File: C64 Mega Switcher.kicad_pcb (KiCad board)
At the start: 2 copper layers, 44.2 x 79.5 mm, 20 parts, among them J1 Port 1, J2 Port 2, J3 Mega Drive, J4 C_SEL, J5 B_SEL, SW1 P1_SEL, SW2 P2_SEL, U1 74HCT4053, U2 74HCT4053, U3 NE555

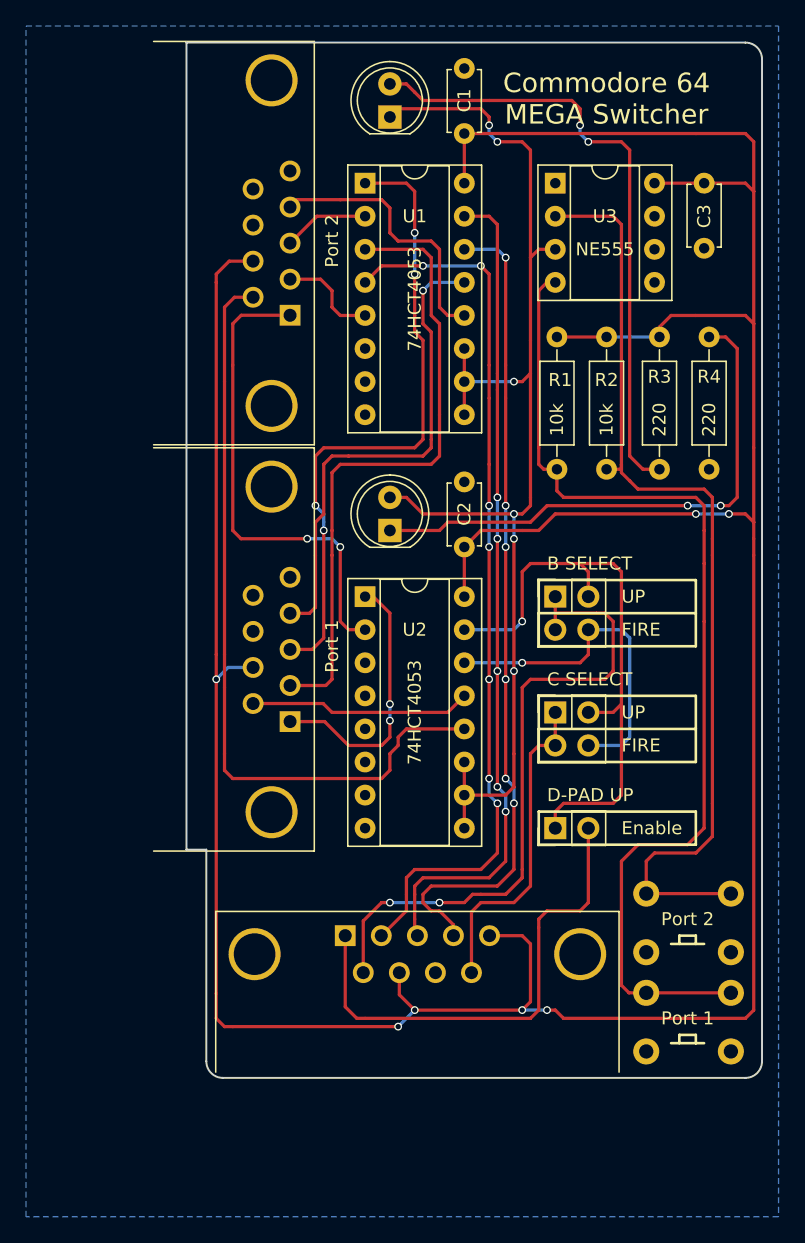
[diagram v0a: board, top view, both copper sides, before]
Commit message: Added protection diodes
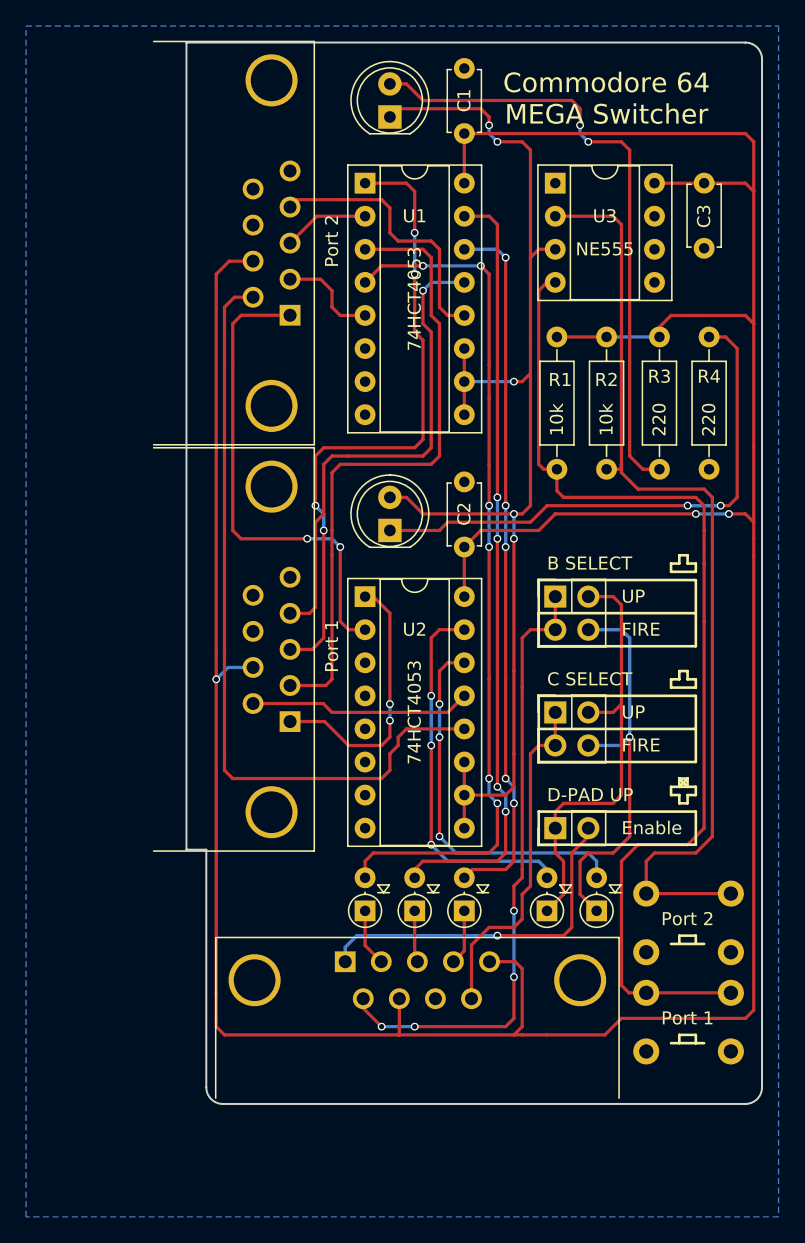
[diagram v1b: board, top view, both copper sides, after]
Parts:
- added D3: 1N4148, Diodes_THT:D_DO-35_SOD27_P2.54mm_Vertical_AnodeUp, F.Cu at (119.4, 102.2)
- added D4: 1N4148, Diodes_THT:D_DO-35_SOD27_P2.54mm_Vertical_AnodeUp, F.Cu at (115.6, 102.2)
- added D5: 1N4148, Diodes_THT:D_DO-35_SOD27_P2.54mm_Vertical_AnodeUp, F.Cu at (111.8, 102.2)
- added D6: 1N4148, Diodes_THT:D_DO-35_SOD27_P2.54mm_Vertical_AnodeUp, F.Cu at (129.5, 102.2)
- added D7: 1N4148, Diodes_THT:D_DO-35_SOD27_P2.54mm_Vertical_AnodeUp, F.Cu at (125.7, 102.2)
- moved J3 2.00 mm to (110.2, 106.1)
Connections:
- J3 pad 2: DOWN -> /MD_D
- J3 pad 3: LEFT -> /MD_L
- J3 pad 4: RIGHT -> /MD_R
- J4 pad 2: UP -> Net-(D7-Pad1)
- J4 pad 4: FIRE -> Net-(D6-Pad1)
- J5 pad 2: UP -> Net-(D7-Pad1)
- J5 pad 4: FIRE -> Net-(D6-Pad1)
- JP1 pad 1: UP -> Net-(D7-Pad1)
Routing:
- net Net-(D7-Pad1): track 0.00 -> 34.2 mm
- net Net-(D6-Pad1): track 0.00 -> 31.1 mm, vias 0 -> 1
- net UP: track 46.3 -> 29.0 mm, vias 1 -> 3
- net /MD_U: track 38.4 -> 27.3 mm, vias 0 -> 1
- net RIGHT: track 63.0 -> 54.4 mm, vias 6 -> 5
- net /MD_D: track 0.00 -> 4.42 mm
- net /MD_R: track 0.00 -> 4.25 mm
- net LEFT: track 63.6 -> 59.5 mm, vias 5 -> 4
- net /MD_L: track 0.00 -> 3.99 mm
- net FIRE: track 26.2 -> 29.0 mm, vias 1 -> 3
- net Net-(J3-Pad6): track 50.7 -> 48.0 mm, vias 2 -> 4
- net DOWN: track 68.1 -> 66.3 mm, vias 7 -> 6
- net Net-(J3-Pad9): track 24.9 -> 26.5 mm
- net VCC: track 263.0 -> 262.2 mm, vias 7 -> 3
- net PORT: vias 6 -> 5
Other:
- board size 44.2 x 79.5 mm -> 44.2 x 81.5 mm

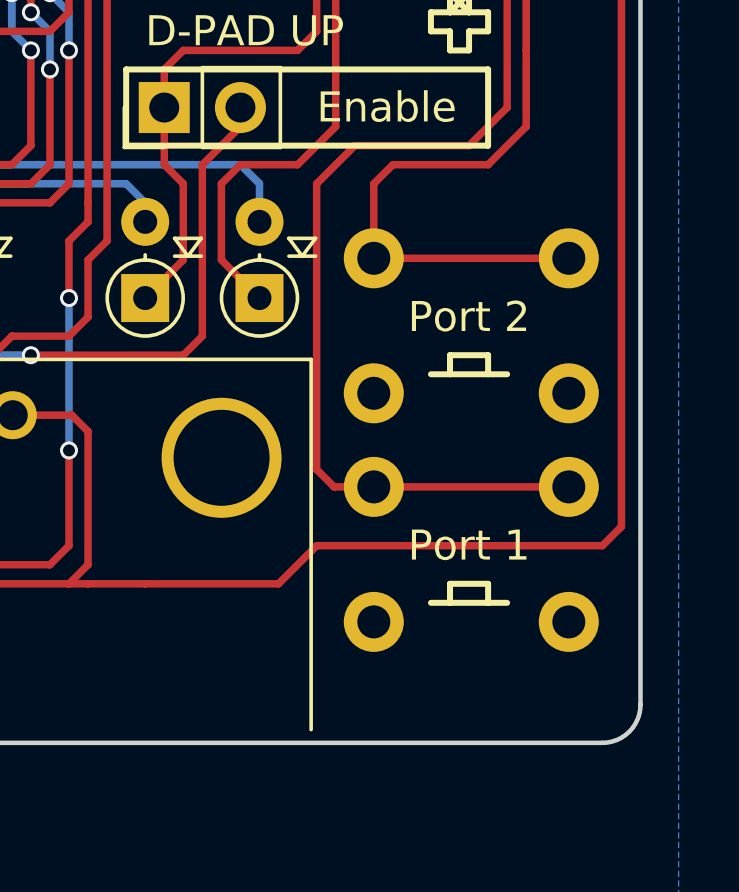
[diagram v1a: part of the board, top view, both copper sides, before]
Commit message: Swapped buttons the right way
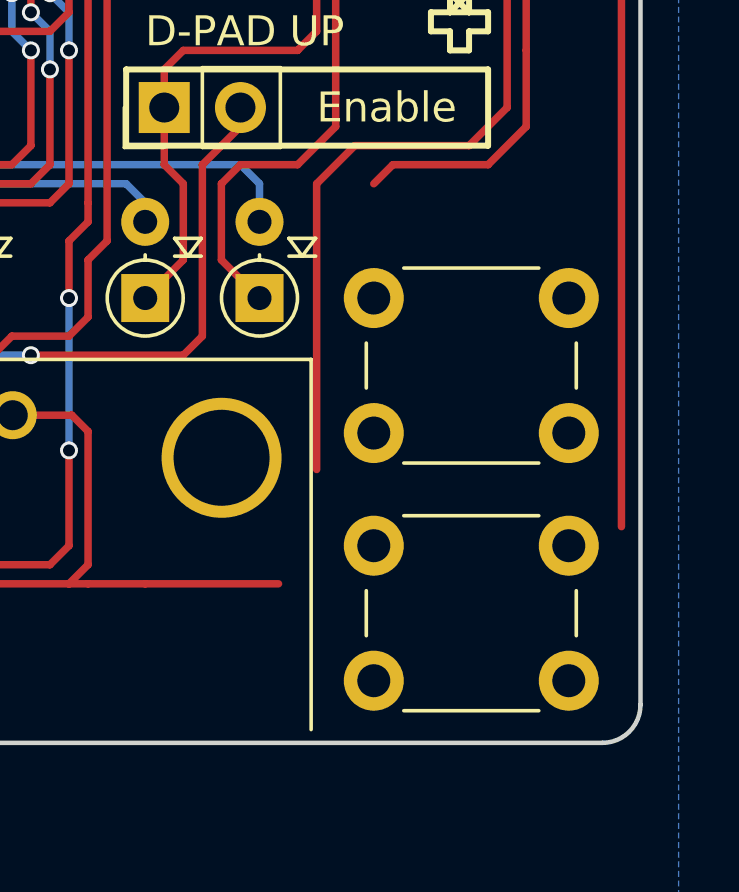
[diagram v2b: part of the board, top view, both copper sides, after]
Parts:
- SW1, SW2: moved to F.Cu
- moved SW2 3.17 mm to (133.3, 102.2)
- moved SW1 2.54 mm to (133.3, 110.5)
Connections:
- SW1 pad 2: Net-(R1-Pad2) -> Net-(R2-Pad2)
- SW2 pad 2: Net-(R2-Pad2) -> Net-(R1-Pad2)
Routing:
- net VCC: track 262.2 -> 250.0 mm
- net Net-(R2-Pad2): track 74.6 -> 65.6 mm
- net Net-(R1-Pad2): track 80.2 -> 71.5 mm
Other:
- board text added: "Licensed under CERN OHL v.1.2 github.com/tebl"
- board text removed: "Licensed under CERN OHL v.1.2"

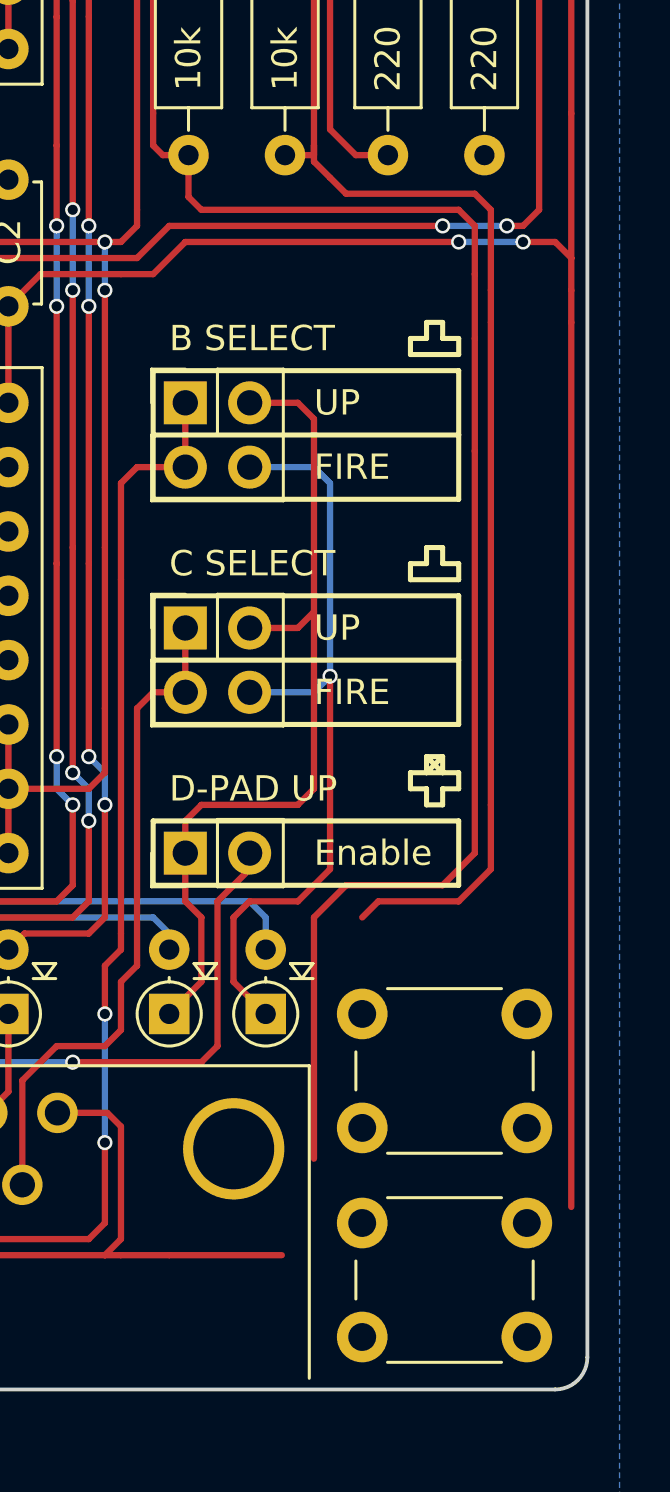
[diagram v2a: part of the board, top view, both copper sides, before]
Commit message: Added tracks to buttons
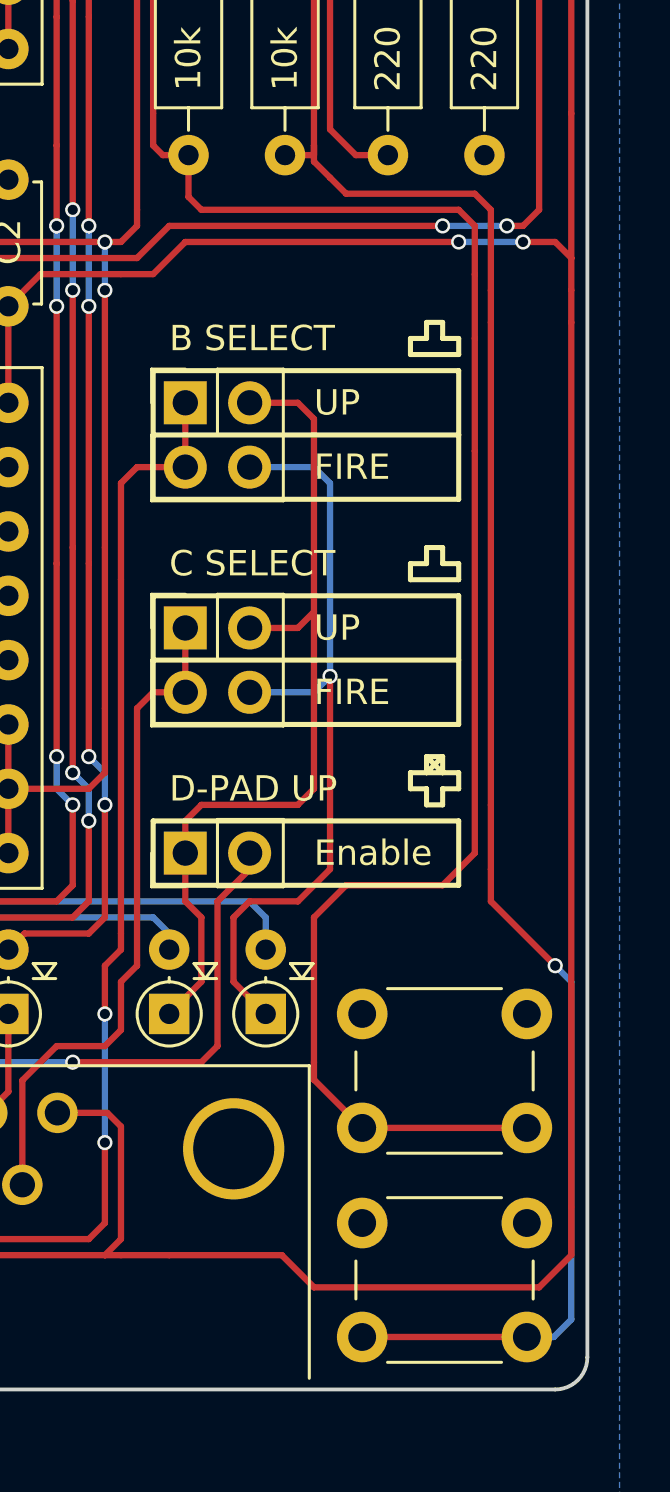
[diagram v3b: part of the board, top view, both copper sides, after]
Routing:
- net Net-(R2-Pad2): track 65.6 -> 87.4 mm, vias 0 -> 1
- net VCC: track 250.0 -> 264.4 mm
- net Net-(R1-Pad2): track 71.5 -> 77.6 mm

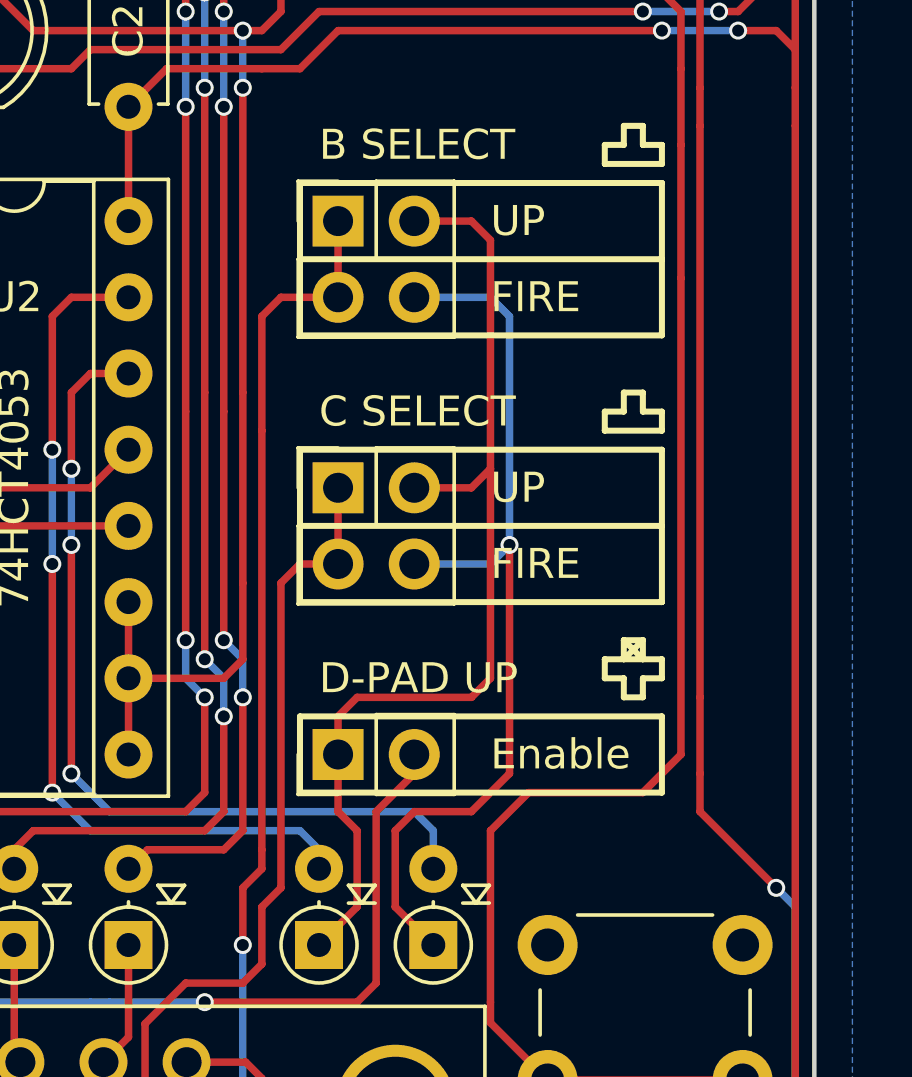
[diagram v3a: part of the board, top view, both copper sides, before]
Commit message: Added silkscreen warnings
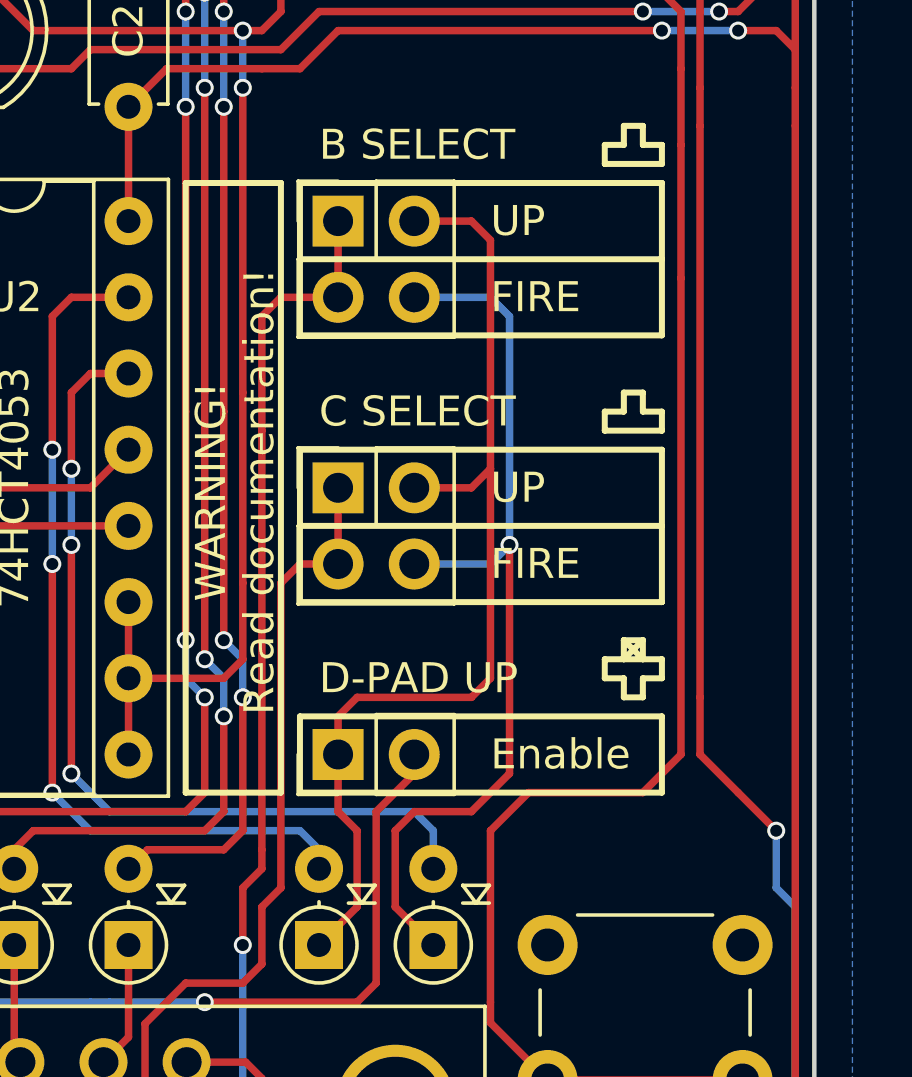
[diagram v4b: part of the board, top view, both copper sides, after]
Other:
- board text added: "Do NOT change when powered, do not jumper any function MORE than ONCE!"
- board text added: "WARNING! Read documentation!"
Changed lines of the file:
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@@
     (links 75)
     (no_connects 0)
-    (area 85.725 34.29 143.510001 125.730001)
+    (area 97.968999 35.484999 142.315001 117.137001)
     (thickness 1.6)
-    (drawings 76)
-    (tracks 447)
+    (drawings 94)
+    (tracks 448)
     (zones 0)
     (modules 25)
@@
       (rotate (xyz 0 0 0))
     )
+  )
+  (gr_line (start 128.905 82.55) (end 128.905 81.915) (angle 90) (layer B.SilkS) (width 0.2))
+  (gr_line (start 126.365 82.55) (end 128.905 82.55) (angle 90) (layer B.SilkS) (width 0.2))
+  (gr_line (start 126.365 81.915) (end 126.365 82.55) (angle 90) (layer B.SilkS) (width 0.2))
+  (gr_line (start 128.905 93.98) (end 128.905 94.615) (angle 90) (layer B.SilkS) (width 0.2))
+  (gr_line (start 126.365 93.98) (end 128.905 93.98) (angle 90) (layer B.SilkS) (width 0.2))
+  (gr_line (start 126.365 94.615) (end 126.365 93.98) (angle 90) (layer B.SilkS) (width 0.2))
+  (gr_line (start 126.365 80.645) (end 128.905 80.645) (angle 90) (layer B.SilkS) (width 0.2))
+  (gr_line (start 126.365 95.885) (end 128.905 95.885) (angle 90) (layer B.SilkS) (width 0.2))
+  (gr_line (start 125.095 97.155) (end 125.095 76.835) (angle 90) (layer B.SilkS) (width 0.2))
+  (gr_line (start 137.16 97.155) (end 125.095 97.155) (angle 90) (layer B.SilkS) (width 0.2))
+  (gr_line (start 137.16 76.835) (end 137.16 97.155) (angle 90) (layer B.SilkS) (width 0.2))
+  (gr_line (start 125.095 76.835) (end 137.16 76.835) (angle 90) (layer B.SilkS) (width 0.2))
+  (gr_text "Do NOT change when\npowered, do not jumper\nany function MORE\nthan ONCE!" (at 133.35 87.63 90) (layer B.SilkS)
+    (effects (font (size 1 1) (thickness 0.15)) (justify mirror))
+  )
+  (gr_line (start 124.46 76.835) (end 124.46 97.155) (angle 90) (layer F.SilkS) (width 0.2))
+  (gr_line (start 121.285 76.835) (end 124.46 76.835) (angle 90) (layer F.SilkS) (width 0.2))
+  (gr_line (start 121.285 97.155) (end 121.285 76.835) (angle 90) (layer F.SilkS) (width 0.2))
+  (gr_line (start 124.46 97.155) (end 121.285 97.155) (angle 90) (layer F.SilkS) (width 0.2))
+  (gr_text "WARNING!\nRead documentation!" (at 122.936 87.122 90) (layer F.SilkS)
+    (effects (font (size 1 1) (thickness 0.15)))
   )
   (gr_line (start 137.16 85.09) (end 137.16 84.455) (angle 90) (layer F.SilkS) (width 0.2))
@@
   (segment (start 126.492 68.326) (end 126.492 69.977) (width 0.25) (layer F.Cu) (net 24))
   (segment (start 137.795 73.025) (end 137.795 75.565) (width 0.25) (layer F.Cu) (net 24))
-  (segment (start 131.445 104.83) (end 133.35 106.735) (width 0.25) (layer F.Cu) (net 24) (status 800000))
-  (segment (start 133.35 106.735) (end 139.85 106.735) (width 0.25) (layer F.Cu) (net 24) (status C00000))
+  (segment (start 131.445 104.83) (end 133.35 106.735) (width 0.25) (layer F.Cu) (net 24))
+  (segment (start 133.35 106.735) (end 139.85 106.735) (width 0.25) (layer F.Cu) (net 24))
   (segment (start 125.095 66.675) (end 125.095 67.945) (width 0.25) (layer F.Cu) (net 24))
   (segment (start 125.476 68.326) (end 126.492 68.326) (width 0.25) (layer F.Cu) (net 24))
@@
   (segment (start 125.095 54.61) (end 125.095 66.675) (width 0.25) (layer F.Cu) (net 24))
   (segment (start 126.365 53.975) (end 125.73 53.975) (width 0.25) (layer F.Cu) (net 24))
-  (segment (start 139.85 114.99) (end 140.915 114.99) (width 0.25) (layer B.Cu) (net 25) (status 400000))
-  (segment (start 138.43 97.79) (end 138.43 96.52) (width 0.25) (layer F.Cu) (net 25))
-  (segment (start 140.97 100.33) (end 138.43 97.79) (width 0.25) (layer F.Cu) (net 25))
-  (via (at 140.97 100.33) (size 0.6) (drill 0.4) (layers F.Cu B.Cu) (net 25))
+  (segment (start 138.43 95.885) (end 139.7 97.155) (width 0.25) (layer F.Cu) (net 25))
+  (segment (start 140.97 98.425) (end 140.97 100.33) (width 0.25) (layer B.Cu) (net 25))
+  (via (at 140.97 98.425) (size 0.6) (drill 0.4) (layers F.Cu B.Cu) (net 25))
+  (segment (start 139.7 97.155) (end 140.97 98.425) (width 0.25) (layer F.Cu) (net 25))
+  (segment (start 139.85 114.99) (end 140.915 114.99) (width 0.25) (layer B.Cu) (net 25))
   (segment (start 141.605 100.965) (end 140.97 100.33) (width 0.25) (layer B.Cu) (net 25))
   (segment (start 141.605 114.3) (end 141.605 100.965) (width 0.25) (layer B.Cu) (net 25))
   (segment (start 140.915 114.99) (end 141.605 114.3) (width 0.25) (layer B.Cu) (net 25))
-  (segment (start 133.35 114.99) (end 139.85 114.99) (width 0.25) (layer F.Cu) (net 25) (status C00000))
+  (segment (start 133.35 114.99) (end 139.85 114.99) (width 0.25) (layer F.Cu) (net 25))
   (segment (start 138.43 74.93) (end 138.43 73.66) (width 0.25) (layer F.Cu) (net 25))
-  (segment (start 138.43 96.52) (end 138.43 93.98) (width 0.25) (layer F.Cu) (net 25))
+  (segment (start 138.43 95.885) (end 138.43 93.98) (width 0.25) (layer F.Cu) (net 25))
   (segment (start 138.43 74.93) (end 138.43 93.98) (width 0.25) (layer F.Cu) (net 25))
   (segment (start 131.445 67.945) (end 131.445 68.58) (width 0.25) (layer F.Cu) (net 25))
